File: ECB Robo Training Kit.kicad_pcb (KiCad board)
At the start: 2 copper layers, 139.6 x 113 mm, 43 parts, among them J1 Ultrsonic, J2 Barrel_Jack_Switch, J3 LCD, J4 DC Motor, K1 Relay SPDT, M1 Servo Motor, Q1 BC547, Q2 BC547, SW1 (D3) Switch 1, SW2 (D4) Switch 2, SW3 (D2) Switch 3, U1 DHT22 (D12), U2 HALL EFFECT, U3 IR, U4 L293D

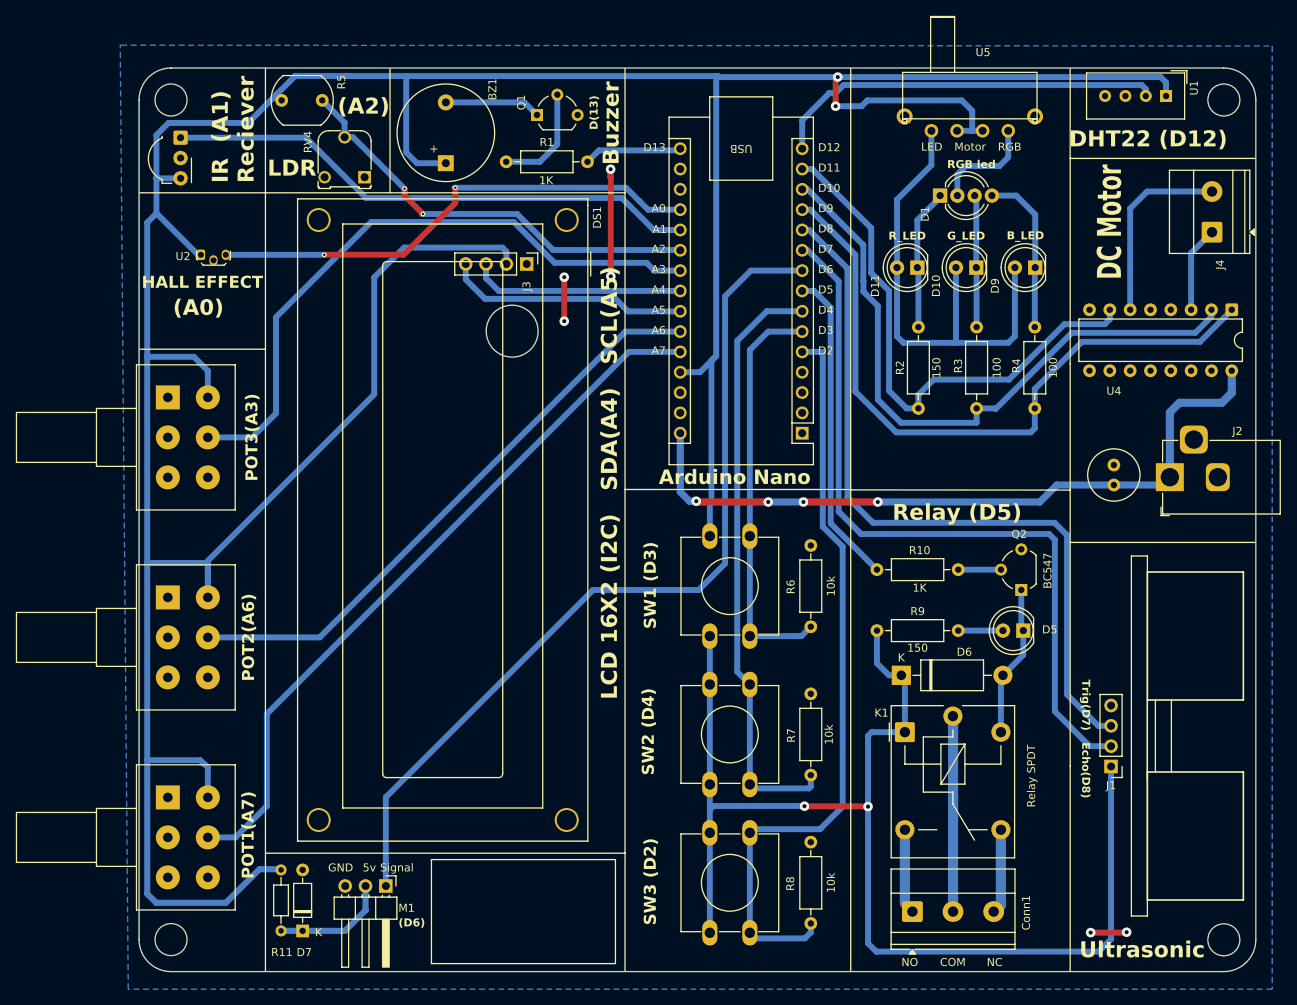
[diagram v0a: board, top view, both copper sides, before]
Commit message: Changed the silkscreen and pin a0 and a2. Added 3d models in the PCB
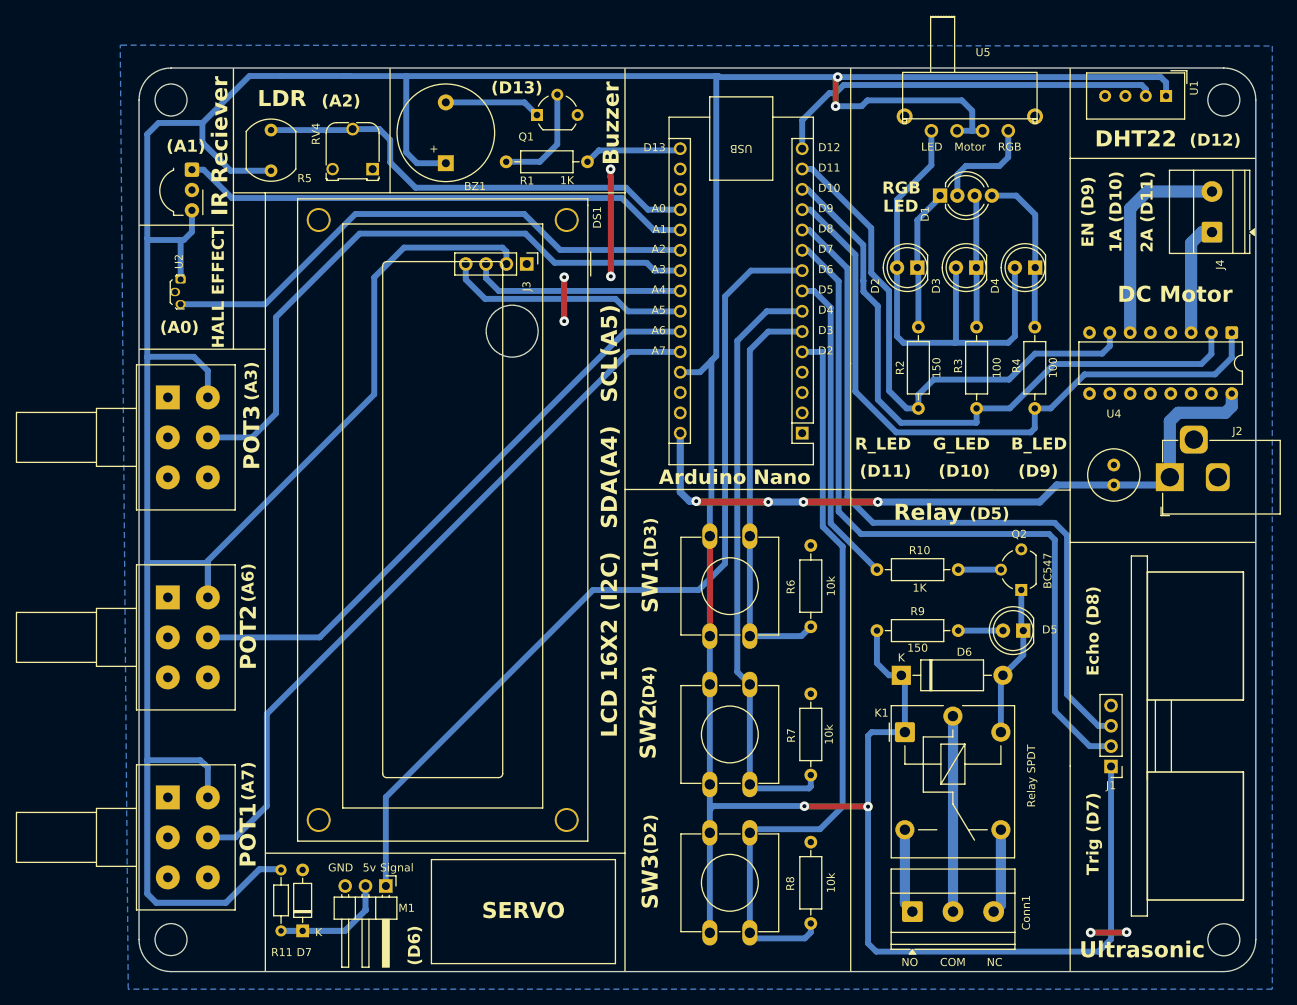
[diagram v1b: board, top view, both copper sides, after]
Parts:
- Conn1: value Relay (D5) -> Relay
- D1: value RGB led -> RGB
- SW1: renamed from SW1 (D3)
- SW2 : renamed from SW2 (D4)
- SW3: renamed from SW3 (D2)
- U1: value DHT22 (D12) -> DHT22
- moved R5 8.89 mm to (114.2, 84.5), turned to 90 degrees
- moved U2 4.40 mm to (102.7, 98.4), turned to -90 degrees
- moved U3 4.25 mm to (104.3, 84.4)
- moved U4 2.86 mm to (234.3, 104.8)
- moved RV4 1.42 mm to (126.9, 84.3)
- renumbered D11 to D2, D10 to D3, D9 to D4, POT1(A7) to POT1, POT2(A6) to POT2, POT3(A3) to POT3
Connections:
- R5 pad 2: /A2 -> /A0
- RV4 pad 2: /A2 -> /A0
- U2 pad 3: /A0 -> /A2
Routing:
- net +5V: track 623.5 -> 652.1 mm
- net /A2: track 54.2 -> 69.0 mm, vias 2 -> 0
- net /A0: track 62.7 -> 57.0 mm, vias 2 -> 0
- net Net-(J4-Pin_1): track 10.8 -> 14.4 mm
- net /A1: track 67.2 -> 64.2 mm
- net Net-(J4-Pin_2): track 23.8 -> 26.6 mm
- net +12V: track 90.5 -> 88.0 mm
- net /A3: track 79.8 -> 78.6 mm
- net /D11: track 68.2 -> 67.3 mm
- net /D9: track 84.5 -> 83.7 mm
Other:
- board text added: "(A1)"
- board text added: "(A3)"
- board text added: "(A6)"
- board text added: "(A7)"
- board text added: "(D10)"
- board text added: "(D11)"
- board text added: "(D12)"
- board text added: "(D13)"
- board text added: "(D2)"
- board text added: "(D3)"
- board text added: "(D4)"
- board text added: "(D5)"
- board text added: "(D9)"
- board text added: "1A (D10)"
- board text added: "2A (D11)"
- board text added: "EN (D9)"
- board text added: "Echo (D8)"
- board text added: "IR Reciever"
- board text added: "SERVO"
- board text added: "Trig (D7)"
- board text removed: "D(13)"
- board text removed: "IR (A1) Reciever"
- board text removed: "Trig(D7) Echo(D8)"
